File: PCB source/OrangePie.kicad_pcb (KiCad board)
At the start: 4 copper layers, 100 x 100 mm, 136 parts, among them J1 09031967921, J2 Orange pi 5 pro, J3 JST XH, J5 Connector, USB-TYPE-C-16P, M1 Fan, Q1 AO3400A, Q2 AO3400A, Q4 AO3400A, Q5 MMBT3904, U1 IP4234CZ6,115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

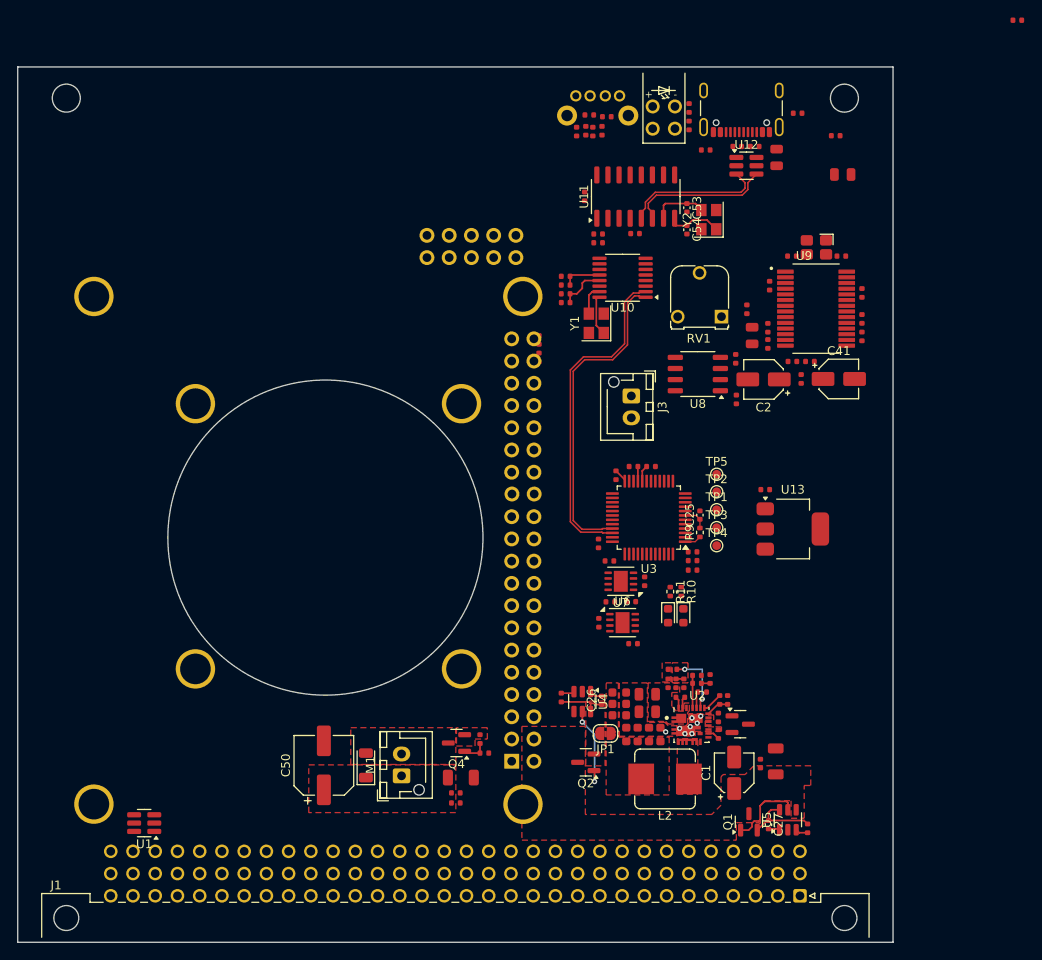
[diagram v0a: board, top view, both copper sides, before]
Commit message: Do signal layer layout
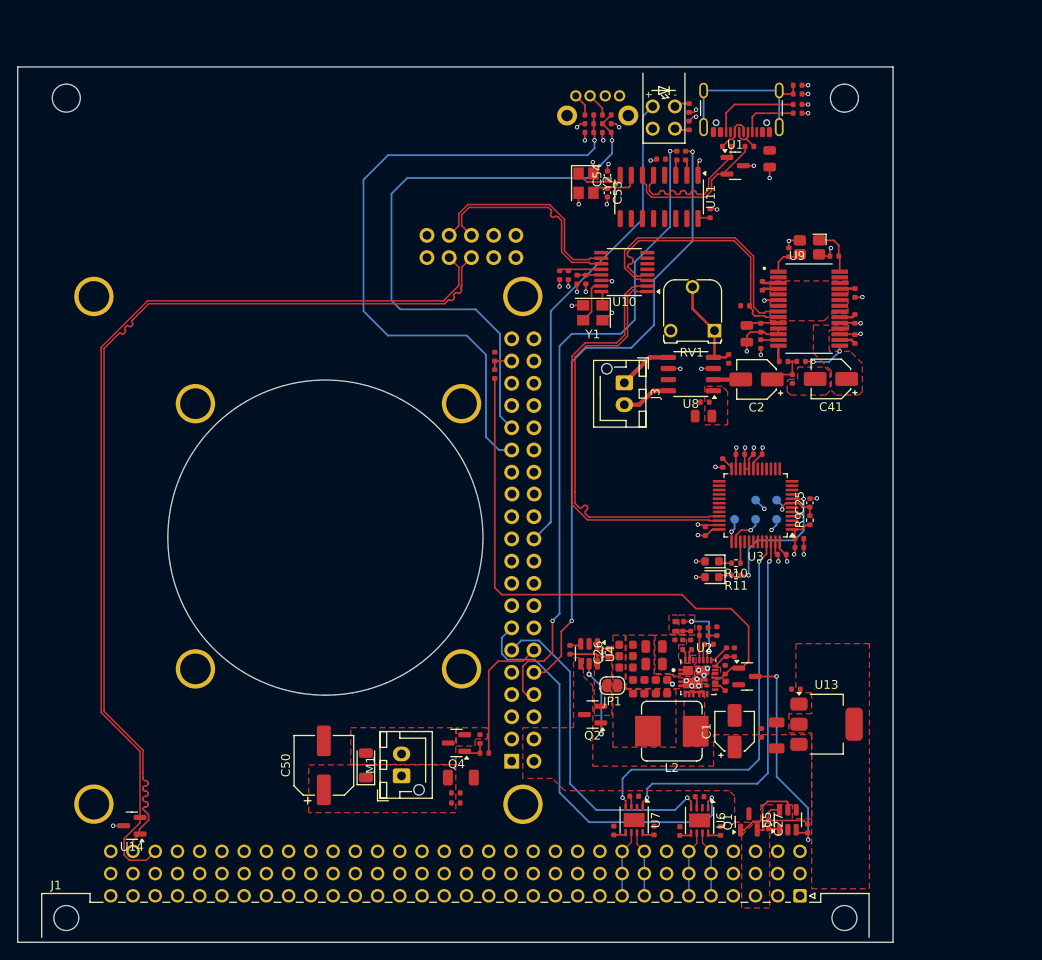
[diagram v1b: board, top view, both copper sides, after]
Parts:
- removed U12: IP4234CZ6, Package_TO_SOT_SMD:SC-74-6_1.55x2.9mm_P0.95mm
- added U14: PESD5V0S2BT, Package_TO_SOT_SMD:SOT-23, F.Cu at (43.7, 125.2)
- TP1, TP2, TP3, TP4, TP5: moved to B.Cu
- U1: value IP4234CZ6,115 -> PESD5V0S2BT; footprint Package_TO_SOT_SMD:SC-74-6_1.55x2.9mm_P0.95mm -> Package_TO_SOT_SMD:SOT-23
- moved U1 101.0 mm to (112.7, 49.8), turned to 0 degrees
- moved C29 30.8 mm to (98.8, 125.7), turned to 90 degrees
- moved R14 28.1 mm to (111.0, 125.8), turned to 90 degrees
- moved U7 27.3 mm to (101.1, 124.5), turned to -90 degrees
- moved R15 26.6 mm to (103.4, 125.8), turned to 90 degrees
- moved C55 26.5 mm to (119.8, 41.6)
- moved C28 24.6 mm to (101.1, 121.8), turned to 180 degrees
- moved U6 24.2 mm to (108.6, 124.6), turned to -90 degrees
- moved C17 23.1 mm to (119.6, 109.6)
- moved C30 23.0 mm to (108.6, 121.9), turned to 180 degrees
- moved U13 22.6 mm to (123.1, 113.6)
- moved C31 22.1 mm to (106.3, 125.8), turned to 90 degrees
- moved C33 21.2 mm to (114.0, 69.0), turned to 90 degrees
- moved Y2 14.6 mm to (95.6, 51.8), turned to -90 degrees
- moved C51 14.5 mm to (109.8, 55.2), turned to 90 degrees
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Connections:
- J1 pad c30: /DIN41612 connector/USB_IN.D- -> /DIN41612 connector/USB_DEBUG.D-
- J1 pad c31: /DIN41612 connector/USB_IN.D+ -> /DIN41612 connector/USB_DEBUG.D+
- R29 pad 2: /Panel USB/USB_IN.D- -> /CH340_DEBUG/FRONT_PANEL.D-
- R30 pad 2: /Panel USB/USB_IN.D+ -> /CH340_DEBUG/FRONT_PANEL.D+
- U1 pad 1: /DIN41612 connector/USB_IN.D- -> /CH340_DEBUG/FRONT_PANEL.D+
- U1 pad 2: GND -> /CH340_DEBUG/FRONT_PANEL.D-
- U1 pad 3: /DIN41612 connector/USB_DEBUG.D- -> GND
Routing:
- net /DIN41612 connector/USB_DEBUG.D-: track 0.00 -> 112.2 mm
- net /DIN41612 connector/USB_DEBUG.D+: track 0.00 -> 111.5 mm
- net /OrangePi 5 pro Header/ON OFF BTN: track 0.00 -> 75.8 mm, vias 0 -> 1
- net /CH340_DEBUG/UART_DEBUG.TX: track 0.00 -> 75.2 mm, vias 0 -> 2
- net /CH340_DEBUG/UART_DEBUG.RX: track 0.00 -> 71.6 mm, vias 0 -> 2
- net /OrangePi 5 pro Header/USER BUTTON: track 0.00 -> 69.9 mm, vias 0 -> 1
- net /5v buck/Pgood: track 0.04 -> 63.4 mm
- net GND: track 0.00 -> 62.1 mm, vias 8 -> 51
- net /OrangePi 5 pro Header/STATUS LED: track 0.00 -> 55.2 mm
- net /Can Transiver/CAN_TR.TXD: track 0.00 -> 46.3 mm, vias 0 -> 1
- net /Can Transiver1/CAN_TR.RXD: track 0.00 -> 45.1 mm, vias 0 -> 2
- net /Can Transiver1/CAN_TR.TXD: track 0.00 -> 43.4 mm, vias 0 -> 2
- net /Can Transiver/CAN_TR.RXD: track 0.00 -> 37.9 mm, vias 0 -> 1
- net /Audio Codec/USB_AUDIO.D-: track 0.00 -> 30.3 mm
- net /Audio Codec/USB_AUDIO.D+: track 0.00 -> 30.3 mm
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- added copper zone on F.Cu, net +3V3
- added copper zone on F.Cu, net /Audio Codec/VDD_{int}
- added copper zone on F.Cu, net /DIN41612 connector/5v_STDBY
- added copper zone on In1.Cu, net GND
- added copper zone on F.Cu, net Net-(U9-VCOM)

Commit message: Finish layout
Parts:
- removed C48: 100nF, PCM_JLCPCB:C_0402
- J5: value Connector, USB-TYPE-C-16P -> USB_C_Receptacle_USB2.0_16P
- moved C49 14.1 mm to (67.3, 121.2)
- moved Q4 14.1 mm to (66.8, 117.2)
- moved R23 14.1 mm to (66.7, 124.1)
- moved R24 14.1 mm to (66.7, 123.0)
- moved R25 14.1 mm to (70.0, 118.4)
- moved R26 14.1 mm to (69.5, 116.8)
- moved C50 14.1 mm to (51.6, 119.8)
- moved M1 14.1 mm to (60.5, 121.0)
- moved D4 14.1 mm to (56.5, 119.8)
- moved C47 1.79 mm to (95.2, 61.5), turned to 180 degrees
- moved RV1 1.68 mm to (110.8, 67.0)
- moved R40 1.10 mm to (85.2, 72.5)
- moved R41 1.10 mm to (85.2, 70.5)
- moved C46 0.72 mm to (95.2, 62.4), turned to 180 degrees
- moved C45 0.72 mm to (95.2, 63.4), turned to 180 degrees
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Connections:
- J5 pad A1: (no net) -> GND
- J5 pad A12: (no net) -> GND
- J5 pad A4: (no net) -> /Panel USB/VBUS_IN
- J5 pad A9: (no net) -> /Panel USB/VBUS_IN
- J5 pad B1: (no net) -> GND
- J5 pad B12: (no net) -> GND
- J5 pad B4: (no net) -> /Panel USB/VBUS_IN
- J5 pad B9: (no net) -> /Panel USB/VBUS_IN
- LED1 pad 3: +5V -> +3V3
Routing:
- net GND: track 62.1 -> 97.6 mm, vias 51 -> 84
- net /5v buck/V_{IN}: track 0.00 -> 26.6 mm, vias 0 -> 17
- net +5V: track 11.3 -> 34.3 mm, vias 0 -> 10
- net /5v buck/5V_OUT: track 2.34 -> 16.8 mm, vias 0 -> 3
- net /FAN controller/FAN_PWM: track 15.5 -> 28.1 mm
- net /Panel USB/VBUS_IN: track 0.00 -> 9.67 mm, vias 0 -> 2
- net /5v buck/5V_VDD: track 1.17 -> 8.15 mm, vias 0 -> 2
- net /USB-CAN/WORD_LED: track 16.1 -> 22.9 mm
- net /Audio Codec/VDD_{int}: track 3.65 -> 9.26 mm, vias 0 -> 2
- net /DIN41612 connector/24v: track 0.00 -> 5.08 mm
- net Net-(Q5-C): track 24.9 -> 29.4 mm
- net +3V3: track 28.4 -> 31.7 mm, vias 10 -> 18
- net /CH340_DEBUG/UART_DEBUG.TX: track 75.2 -> 72.0 mm
- net /5v buck/Pgood: track 63.4 -> 66.0 mm
- net /OrangePi 5 pro Header/USB_OUT.D+: track 24.4 -> 21.8 mm
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- added copper zone on In2.Cu, net +3V3
- added copper zone on In2.Cu, net +5V
- added copper zone on In2.Cu, net /5v buck/V_{IN}
- added copper zone on In2.Cu, net GND
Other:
- outline, holes or cut-outs redrawn

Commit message: Add silk
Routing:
- net /5v buck/V_{IN}: track 26.6 -> 24.4 mm

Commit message: Change speaker holes position
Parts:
- added REF**: ESD-Logo_6.6x6mm_SilkScreen, Symbol:ESD-Logo_6.6x6mm_SilkScreen, F.Cu at (122.3, 100.1)
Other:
- outline, holes or cut-outs redrawn
- board text added: "${CURRENT_DATE}"
- board text added: "${TITLE} ${COMMENT2}"
- board text added: "BRD SHA: %%%%%%%%"
- board text added: "Dominik Pluta Artem Horiunov"
- board text added: "ModuCard System"
- board text added: "PROJECT Rev. ${REVISION} TEMPLATE Rev. 1.0.0"
- board text added: "Project info:"
- board text added: "Template authors:"
